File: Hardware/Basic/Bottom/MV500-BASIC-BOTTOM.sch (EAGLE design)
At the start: 31 parts, among them U1 AD5242-SO16

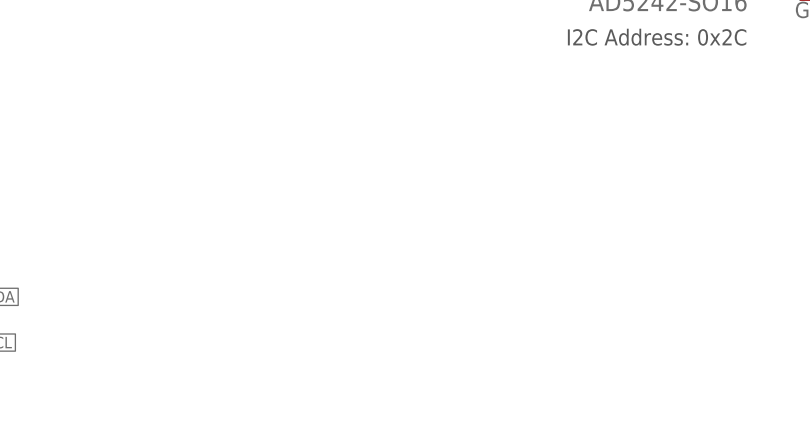
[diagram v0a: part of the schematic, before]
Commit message: Bottom Schematic Updated
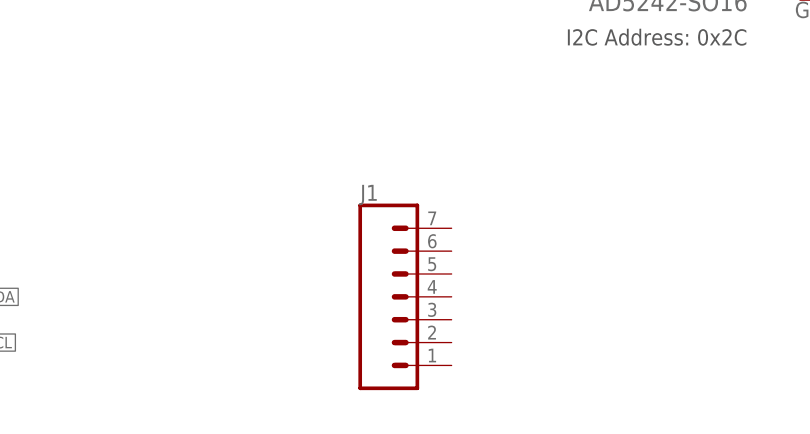
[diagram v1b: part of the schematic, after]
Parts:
- added J1: (no value), LinnesLab-Connectors:CONN_07
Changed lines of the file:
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@@
 <part name="GND30" library="LinnesLab-Symbols" deviceset="GND" device=""/>
 <part name="SUPPLY24" library="LinnesLab-Symbols" deviceset="3.3V" device=""/>
+<part name="J1" library="LinnesLab-Connectors" deviceset="CONN_07" device=""/>
 </parts>
 <sheets>
@@
 <attribute name="VALUE" x="45.72" y="35.814" size="1.778" layer="96" align="bottom-center"/>
 </instance>
+<instance part="J1" gate="G$1" x="134.62" y="25.4" smashed="yes">
+<attribute name="VALUE" x="129.54" y="15.494" size="1.778" layer="96" font="vector"/>
+<attribute name="NAME" x="129.54" y="38.608" size="1.778" layer="95" font="vector"/>
+</instance>
 </instances>

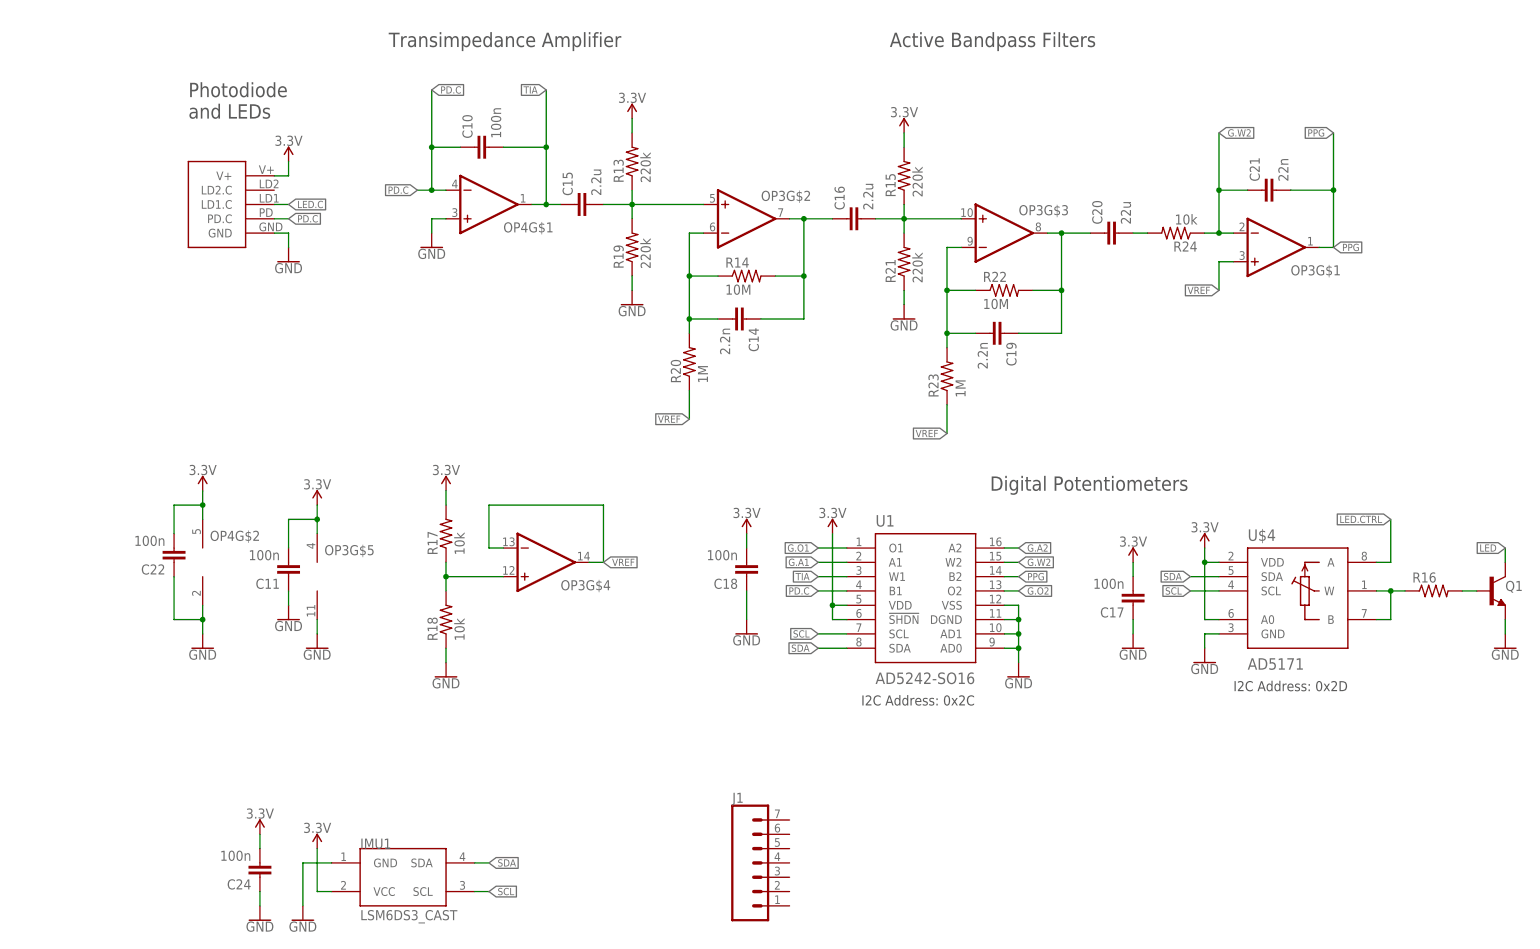
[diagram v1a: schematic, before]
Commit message: Updated Bottom Schematic
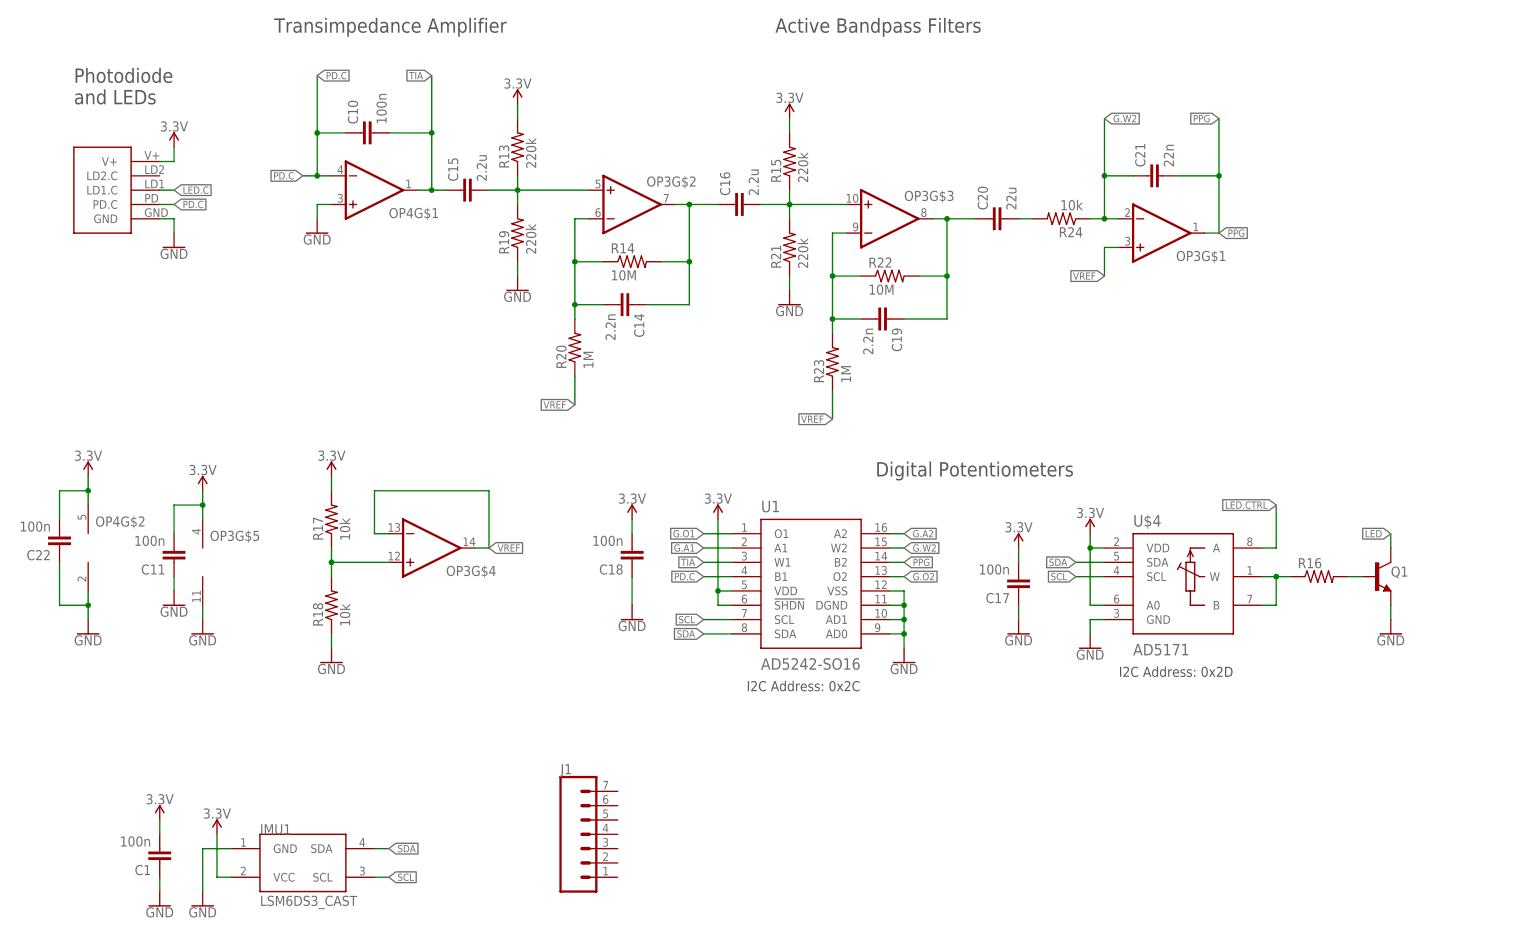
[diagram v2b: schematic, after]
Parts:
- removed C24: 100n, LinnesLab-Passives:CAPACITOR0603
- added C1: 100n, LinnesLab-Passives:CAPACITOR0603
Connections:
- net 3.3V: now also C1.2; no longer C24.2
- net GND: now also C1.1; no longer C24.1
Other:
- moved on the sheet: C10, C11, C14, C15, C16, C17, C18, C19, C20, C21, C22, IMU1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
